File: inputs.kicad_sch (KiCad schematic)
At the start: 44 parts, among them IC3 Trig Cond Socket, U5 MPX4250, U6 SP720

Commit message: Populate Board
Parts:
- removed C15: 0.01uF, Capacitor_SMD:C_0805_2012Metric, symbol Device:C
- removed C16: 0.1uF, Capacitor_SMD:C_0805_2012Metric, symbol Device:C
- removed C29, C8: 470pf, Capacitor_SMD:C_0805_2012Metric, symbol Device:C
- removed JP4, JP5: PULL-UP, Connector_PinHeader_2.54mm:PinHeader_1x02_P2.54mm_Vertical, symbol Jumper:Jumper_2_Open
- removed R34, R55: 470R, Resistor_SMD:R_0805_2012Metric, symbol Device:R
- added C18: 0.01uF, Capacitor_SMD:C_0805_2012Metric, symbol Device:C
- added C19: 0.1uF, Capacitor_SMD:C_0805_2012Metric, symbol Device:C
- added C5, C6: 470pf, Capacitor_SMD:C_0805_2012Metric, symbol Device:C
- added JP2, JP3: PULL-UP, Connector_PinHeader_2.54mm:PinHeader_1x02_P2.54mm_Vertical, symbol Jumper:Jumper_2_Open
- JP1: renamed from JP11; footprint Jumper:SolderJumper-3_P1.3mm_Bridged12_RoundedPad1.0x1.5mm -> Jumper:SolderJumper-3_P1.3mm_Open_RoundedPad1.0x1.5mm
- renumbered C7 to C10, C5 to C11, C9 to C12, C12 to C13, C10 to C14, C13 to C15, C11 to C16, C14 to C17, C1 to C3, C2 to C4, C3 to C7, C6 to C8, C4 to C9, D20 to D2, D13 to D3, IC3 to IC1, JP2 to JP4, JP3 to JP5, R31 to R30, R29 to R31, R30 to R32, R32 to R33, R33 to R34, R38 to R35, R35 to R36, R39 to R37, R36 to R38, R40 to R39, R37 to R40
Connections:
- net ADC-Clamp-14 is gone; now on net RAW-BAT-REF: U6.15 (I14)
- net CAM-IN: now also JP3.2 (B)
- net CRANK-IN: now also JP2.1 (A)
- net GND: now also C3.2, C4.2, C18.2, C19.2, C5.2, C6.1; no longer C3.1, C4.1
- net at R41.1: now also JP2.2 (B)
- net +5VA: now reaches R42.1
- net +5VA: now also IC1.5 (Pin_5), R34.1, R36.2, R38.2, R41.2, U6.16 (V+)
- net RAW-BARO-IN: now reaches JP1.3 (B)
- net RAW-BARO-IN: now also U6.11 (I10), C6.2
- net 12V-SW renamed +12V
- net ADC-Clamp-1 renamed RAW-BAT-REF
- net RAW-BAT-REF: no longer U6.1 (I1)
- net ADC-Clamp-10 renamed RAW-FLEX-IN
- net RAW-FLEX-IN: no longer U6.11 (I10)
- net ADC-Clamp-11 renamed RAW-O2
- net RAW-O2: now also C8.1, R30.1
- net ADC-Clamp-12 renamed RAW-CAM-IN
- net RAW-CAM-IN: now also IC1.7 (Pin_7), R44.1, C19.1
- net ADC-Clamp-13 renamed RAW-CLUTCH
- net RAW-CLUTCH: now also U6.1 (I1); no longer U6.14 (I13)
- net ADC-Clamp-2 renamed RAW-COOLANT
- net RAW-COOLANT: now also C17.1, R39.1
- removed net ADC-Clamp-3: C17.1, R39.1, U6.3 (I3)
- net ADC-Clamp-4 renamed RAW-TPS
- net ADC-Clamp-5 renamed RAW-IAT
- net RAW-IAT: now also U6.14 (I13); no longer U6.5 (I5)
- removed net ADC-Clamp-6: C8.1, R30.1, U6.6 (I6)
- net ADC-Clamp-7: no longer names the net of U6.7 (I7)
- removed net ADC-Clamp-8: IC1.7 (Pin_7), R44.1, U6.9 (I8)
- net ADC-Clamp-9 renamed RAW-CRANK-IN
- net RAW-CRANK-IN: now also U6.3 (I3), C18.1; no longer U6.10 (I9)
- net CLT_Sensor renamed COOLANT-IN
- net Clutch_in renamed CLUTCH-IN
- net IAT_Sensor renamed IAT-IN
- net MAP-EXT renamed RAW-MAP-IN
- net RAW-MAP-IN: now also U6.6 (I6), C5.1
- net O2_Sensor renamed O2-IN
- net TPS_Sensor renamed TPS-IN
- removed net VDD: C3.2, C4.2, IC1.5 (Pin_5), U5.3 (VCC)
- removed net VDDA: R34.1, R36.2, R38.2, R41.2, R42.2, U6.16 (V+)
- new net: JP3.1 (A), R42.2
- new net +5V: C3.1, C4.1, U5.3 (VCC)
- new net RAW-FLEX: U6.5 (I5)
- no-connect marks 0 -> 3
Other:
- note added: "Surge Protection"
- moved on the sheet: C10, C12, C13, C14, C15, C16, C17, C3, C4, C7, C8, C9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

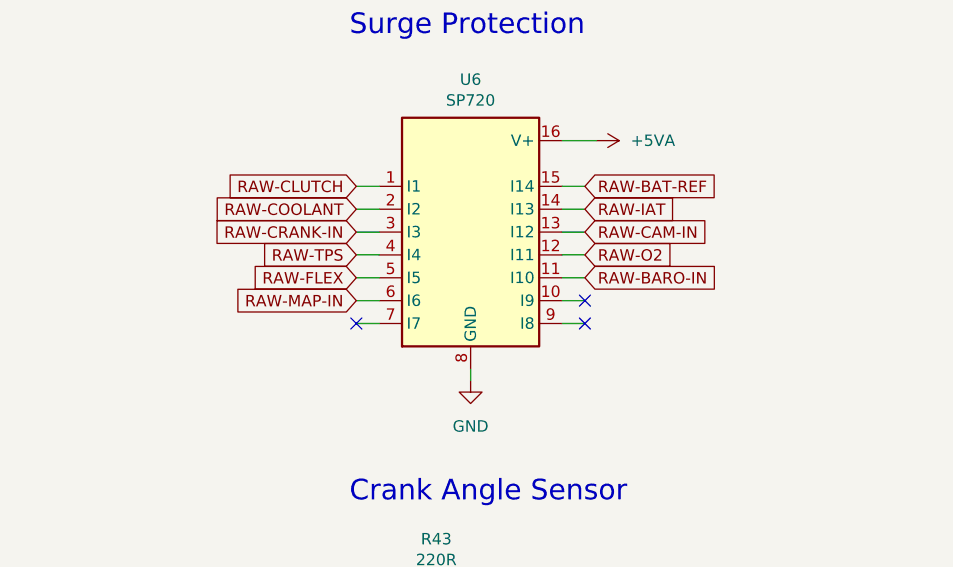
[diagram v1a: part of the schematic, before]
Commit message: Add additional IOs
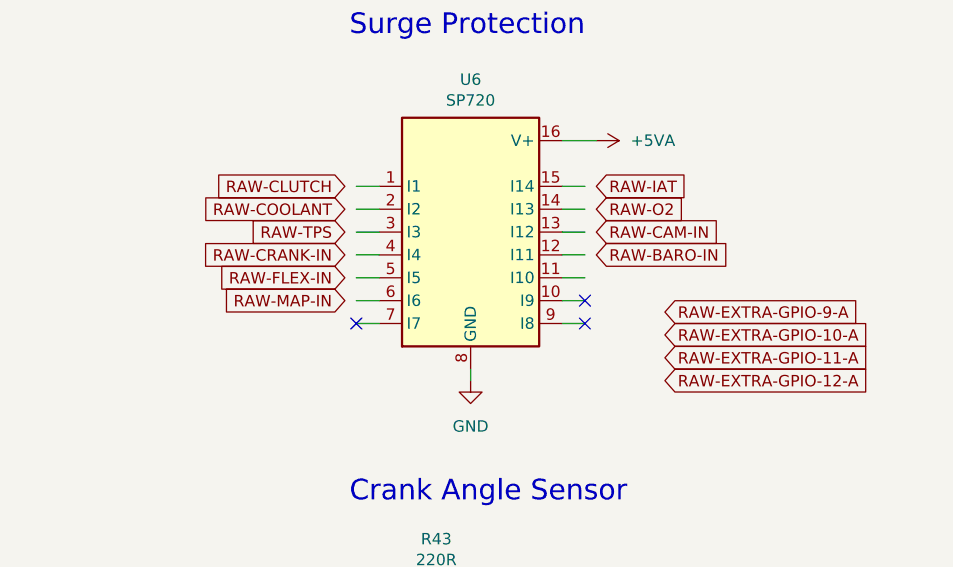
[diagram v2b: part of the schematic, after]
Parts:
- JP2, JP3: footprint Connector_PinHeader_2.54mm:PinHeader_1x02_P2.54mm_Vertical -> Jumper:SolderJumper-2_P1.3mm_Open_RoundedPad1.0x1.5mm
- JP4, JP5: footprint Connector_PinHeader_2.54mm:PinHeader_1x03_P2.54mm_Vertical -> Jumper:SolderJumper-3_P1.3mm_Open_RoundedPad1.0x1.5mm
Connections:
- net RAW-BARO-IN: no longer U6.11 (I10)
- net RAW-BAT-REF: no longer U6.15 (I14)
- net RAW-CAM-IN: no longer U6.13 (I12)
- net RAW-CLUTCH: no longer U6.1 (I1)
- net RAW-COOLANT: no longer U6.2 (I2)
- net RAW-CRANK-IN: no longer U6.3 (I3)
- net RAW-IAT: no longer U6.14 (I13)
- net RAW-MAP-IN: no longer U6.6 (I6)
- net RAW-O2: no longer U6.12 (I11)
- net RAW-TPS: no longer U6.4 (I4)
- net RAW-FLEX: no longer names the net of U6.5 (I5)
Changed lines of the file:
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@@
 		)
 	)
-	(global_label "RAW-CRANK-IN"
+	(global_label "RAW-BARO-IN"
 		(shape input)
-		(at 215.9 48.26 180)
+		(at 242.57 50.8 0)
 		(effects
 			(font
 				(size 1.27 1.27)
 			)
-			(justify right)
+			(justify left)
 		)
 		(property "Intersheetrefs" "${INTERSHEET_REFS}"
-			(at 215.9 48.26 0)
+			(at 242.57 50.8 0)
 			(effects
 				(font
@@
 		)
 	)
-	(global_label "RAW-CLUTCH"
+	(global_label "RAW-BAT-REF"
 		(shape input)
-		(at 215.9 43.18 180)
+		(at 72.39 128.27 0)
 		(effects
 			(font
 				(size 1.27 1.27)
 			)
-			(justify right)
+			(justify left)
 		)
 		(property "Intersheetrefs" "${INTERSHEET_REFS}"
-			(at 215.9 43.18 0)
+			(at 72.39 128.27 0)
 			(effects
 				(font
@@
 		)
 	)
-	(global_label "RAW-MAP-IN"
+	(global_label "RAW-COOLANT"
 		(shape input)
-		(at 215.9 55.88 180)
+		(at 214.63 45.72 180)
 		(effects
 			(font
@@
 		)
 		(property "Intersheetrefs" "${INTERSHEET_REFS}"
-			(at 215.9 55.88 0)
+			(at 214.63 45.72 0)
 			(effects
 				(font
 					(size 1.27 1.27)
 				)
-				(justify left)
 				(hide yes)
 			)
 		)
 	)
-	(global_label "RAW-IAT"
+	(global_label "RAW-COOLANT"
 		(shape input)
-		(at 241.3 45.72 0)
+		(at 144.78 125.73 0)
 		(effects
 			(font
@@
 		)
 		(property "Intersheetrefs" "${INTERSHEET_REFS}"
-			(at 241.3 45.72 0)
+			(at 144.78 125.73 0)
 			(effects
 				(font
 					(size 1.27 1.27)
 				)
-				(justify right)
 				(hide yes)
 			)
 		)
 	)
-	(global_label "RAW-COOLANT"
+	(global_label "VR1-"
 		(shape input)
-		(at 144.78 125.73 0)
+		(at 229.87 102.87 180)
 		(effects
 			(font
 				(size 1.27 1.27)
 			)
-			(justify left)
+			(justify right)
 		)
 		(property "Intersheetrefs" "${INTERSHEET_REFS}"
-			(at 144.78 125.73 0)
+			(at 229.87 102.87 0)
 			(effects
 				(font
@@
 		)
 	)
-	(global_label "RAW-CAM-IN"
+	(global_label "RAW-CRANK-IN"
 		(shape input)
-		(at 241.3 48.26 0)
+		(at 214.63 50.8 180)
 		(effects
 			(font
 				(size 1.27 1.27)
 			)
-			(justify left)
+			(justify right)
 		)
 		(property "Intersheetrefs" "${INTERSHEET_REFS}"
-			(at 241.3 48.26 0)
+			(at 214.63 50.8 0)
 			(effects
 				(font
 					(size 1.27 1.27)
 				)
-				(justify left)
+				(justify right)
 				(hide yes)
 			)
 		)
 	)
-	(global_label "VR1-"
+	(global_label "RAW-CLUTCH"
 		(shape input)
-		(at 229.87 102.87 180)
+		(at 140.97 165.1 0)
 		(effects
 			(font
 				(size 1.27 1.27)
 			)
-			(justify right)
+			(justify left)
 		)
 		(property "Intersheetrefs" "${INTERSHEET_REFS}"
-			(at 229.87 102.87 0)
+			(at 140.97 165.1 0)
 			(effects
 				(font
@@
 		)
 	)
-	(global_label "RAW-O2"
+	(global_label "RAW-EXTRA-GPIO-10-A"
 		(shape input)
-		(at 241.3 50.8 0)
+		(at 250.19 59.69 0)
 		(effects
 			(font
@@
 		)
 		(property "Intersheetrefs" "${INTERSHEET_REFS}"
-			(at 241.3 50.8 0)
+			(at 250.19 59.69 0)
 			(effects
 				(font
 					(size 1.27 1.27)
 				)
-				(justify right)
 				(hide yes)
 			)
@@
 	(global_label "RAW-CLUTCH"
 		(shape input)
-		(at 140.97 165.1 0)
+		(at 214.63 43.18 180)
 		(effects
 			(font
 				(size 1.27 1.27)
 			)
-			(justify left)
+			(justify right)
 		)
 		(property "Intersheetrefs" "${INTERSHEET_REFS}"
-			(at 140.97 165.1 0)
+			(at 214.63 43.18 0)
 			(effects
 				(font
@@
 		)
 	)
-	(global_label "RAW-BARO-IN"
+	(global_label "IAT-IN"
 		(shape input)
-		(at 241.3 53.34 0)
+		(at 116.84 78.74 180)
 		(effects
 			(font
 				(size 1.27 1.27)
 			)
-			(justify left)
+			(justify right)
 		)
 		(property "Intersheetrefs" "${INTERSHEET_REFS}"
-			(at 241.3 53.34 0)
+			(at 116.84 78.74 0)
 			(effects
 				(font
 					(size 1.27 1.27)
 				)
-				(justify right)
 				(hide yes)
 			)
 		)
 	)
-	(global_label "IAT-IN"
+	(global_label "RAW-EXTRA-GPIO-12-A"
 		(shape input)
-		(at 116.84 78.74 180)
+		(at 250.19 64.77 0)
 		(effects
 			(font
 				(size 1.27 1.27)
 			)
-			(justify right)
+			(justify left)
 		)
 		(property "Intersheetrefs" "${INTERSHEET_REFS}"
-			(at 116.84 78.74 0)
+			(at 250.19 64.77 0)
 			(effects
 				(font
@@
 		)
 	)
-	(global_label "RAW-BAT-REF"
+	(global_label "RAW-EXTRA-GPIO-11-A"
 		(shape input)
-		(at 72.39 128.27 0)
+		(at 250.19 62.23 0)
 		(effects
 			(font
@@
 		)
 		(property "Intersheetrefs" "${INTERSHEET_REFS}"
-			(at 72.39 128.27 0)
+			(at 250.19 62.23 0)
 			(effects
 				(font
@@
 		)
 	)
-	(global_label "RAW-BAT-REF"
+	(global_label "RAW-CAM-IN"
 		(shape input)
-		(at 241.3 43.18 0)
+		(at 242.57 48.26 0)
 		(effects
 			(font
@@
 		)
 		(property "Intersheetrefs" "${INTERSHEET_REFS}"
-			(at 241.3 43.18 0)
+			(at 242.57 48.26 0)
+			(effects
+				(font
+					(size 1.27 1.27)
+				)
+				(justify left)
+				(hide yes)
+			)
+		)
+	)
+	(global_label "RAW-FLEX-IN"
+		(shape input)
+		(at 214.63 53.34 180)
+		(effects
+			(font
+				(size 1.27 1.27)
+			)
+			(justify right)
+		)
+		(property "Intersheetrefs" "${INTERSHEET_REFS}"
+			(at 214.63 53.34 0)
 			(effects
 				(font
 					(size 1.27 1.27)
 				)
-				(justify right)
 				(hide yes)
 			)
@@
 		)
 	)
-	(global_label "RAW-FLEX"
+	(global_label "RAW-TPS"
 		(shape input)
-		(at 215.9 53.34 180)
+		(at 214.63 48.26 180)
 		(effects
 			(font
@@
 		)
 		(property "Intersheetrefs" "${INTERSHEET_REFS}"
-			(at 215.9 53.34 0)
+			(at 214.63 48.26 0)
 			(effects
 				(font
 					(size 1.27 1.27)
 				)
+				(justify left)
 				(hide yes)
 			)
@@
 		)
 	)
-	(global_label "RAW-TPS"
+	(global_label "RAW-O2"
 		(shape input)
-		(at 215.9 50.8 180)
+		(at 242.57 45.72 0)
 		(effects
 			(font
 				(size 1.27 1.27)
 			)
-			(justify right)
+			(justify left)
 		)
 		(property "Intersheetrefs" "${INTERSHEET_REFS}"
-			(at 215.9 50.8 0)
+			(at 242.57 45.72 0)
 			(effects
 				(font
 					(size 1.27 1.27)
 				)
-				(justify left)
+				(justify right)
 				(hide yes)
 			)
@@
 		)
 	)
+	(global_label "RAW-EXTRA-GPIO-9-A"
+		(shape input)
+		(at 250.19 57.15 0)
+		(effects
+			(font
+				(size 1.27 1.27)
+			)
+			(justify left)
+		)
+		(property "Intersheetrefs" "${INTERSHEET_REFS}"
+			(at 250.19 57.15 0)
+			(effects
+				(font
+					(size 1.27 1.27)
+				)
+				(hide yes)
+			)
+		)
+	)
 	(global_label "COOLANT-IN"
 		(shape input)
@@
 		)
 	)
+	(global_label "RAW-MAP-IN"
+		(shape input)
+		(at 214.63 55.88 180)
+		(effects
+			(font
+				(size 1.27 1.27)
+			)
+			(justify right)
+		)
+		(property "Intersheetrefs" "${INTERSHEET_REFS}"
+			(at 214.63 55.88 0)
+			(effects
+				(font
+					(size 1.27 1.27)
+				)
+				(justify left)
+				(hide yes)
+			)
+		)
+	)
 	(global_label "RAW-IAT"
 		(shape input)
@@
 		)
 	)
-	(global_label "RAW-COOLANT"
+	(global_label "RAW-IAT"
 		(shape input)
-		(at 215.9 45.72 180)
+		(at 242.57 43.18 0)
 		(effects
 			(font
 				(size 1.27 1.27)
 			)
-			(justify right)
+			(justify left)
 		)
 		(property "Intersheetrefs" "${INTERSHEET_REFS}"
-			(at 215.9 45.72 0)
+			(at 242.57 43.18 0)
 			(effects
 				(font
 					(size 1.27 1.27)
 				)
+				(justify right)
 				(hide yes)
 			)
@@
 			)
 		)
-		(property "Footprint" "Connector_PinHeader_2.54mm:PinHeader_1x03_P2.54mm_Vertical"
+		(property "Footprint" "Jumper:SolderJumper-3_P1.3mm_Open_RoundedPad1.0x1.5mm"
 			(at 218.44 96.52 0)
 			(effects
@@
 			)
 		)
-		(property "Footprint" "Connector_PinHeader_2.54mm:PinHeader_1x03_P2.54mm_Vertical"
+		(property "Footprint" "Jumper:SolderJumper-3_P1.3mm_Open_RoundedPad1.0x1.5mm"
 			(at 218.44 116.84 0)
 			(effects
@@
 			)
 		)
-		(property "Footprint" "Connector_PinHeader_2.54mm:PinHeader_1x02_P2.54mm_Vertical"
+		(property "Footprint" "Jumper:SolderJumper-2_P1.3mm_Open_RoundedPad1.0x1.5mm"
 			(at 204.47 116.84 0)
 			(effects
@@
 			)
 		)
-		(property "Footprint" "Connector_PinHeader_2.54mm:PinHeader_1x02_P2.54mm_Vertical"
+		(property "Footprint" "Jumper:SolderJumper-2_P1.3mm_Open_RoundedPad1.0x1.5mm"
 			(at 204.47 96.52 0)
 			(effects

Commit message: Pre MCU switch
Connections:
- net RAW-BARO-IN: now also U6.7 (I7)
- net RAW-CAM-IN: now also U6.5 (I5)
- net RAW-CLUTCH: now also U6.10 (I9)
- net RAW-COOLANT: now also U6.3 (I3)
- net RAW-CRANK-IN: now also U6.4 (I4)
- net RAW-EXTRA-GPIO-10-A: now also U6.13 (I12)
- net RAW-EXTRA-GPIO-11-A: now also U6.14 (I13)
- net RAW-EXTRA-GPIO-12-A: now also U6.15 (I14)
- net RAW-EXTRA-GPIO-9-A: now also U6.12 (I11)
- net RAW-FLEX-IN: now also U6.2 (I2)
- net RAW-IAT: now also U6.11 (I10)
- net RAW-MAP-IN: now also U6.6 (I6)
- net RAW-O2: now also U6.1 (I1)
- net RAW-TPS: now also U6.9 (I8)
- no-connect marks 3 -> 0

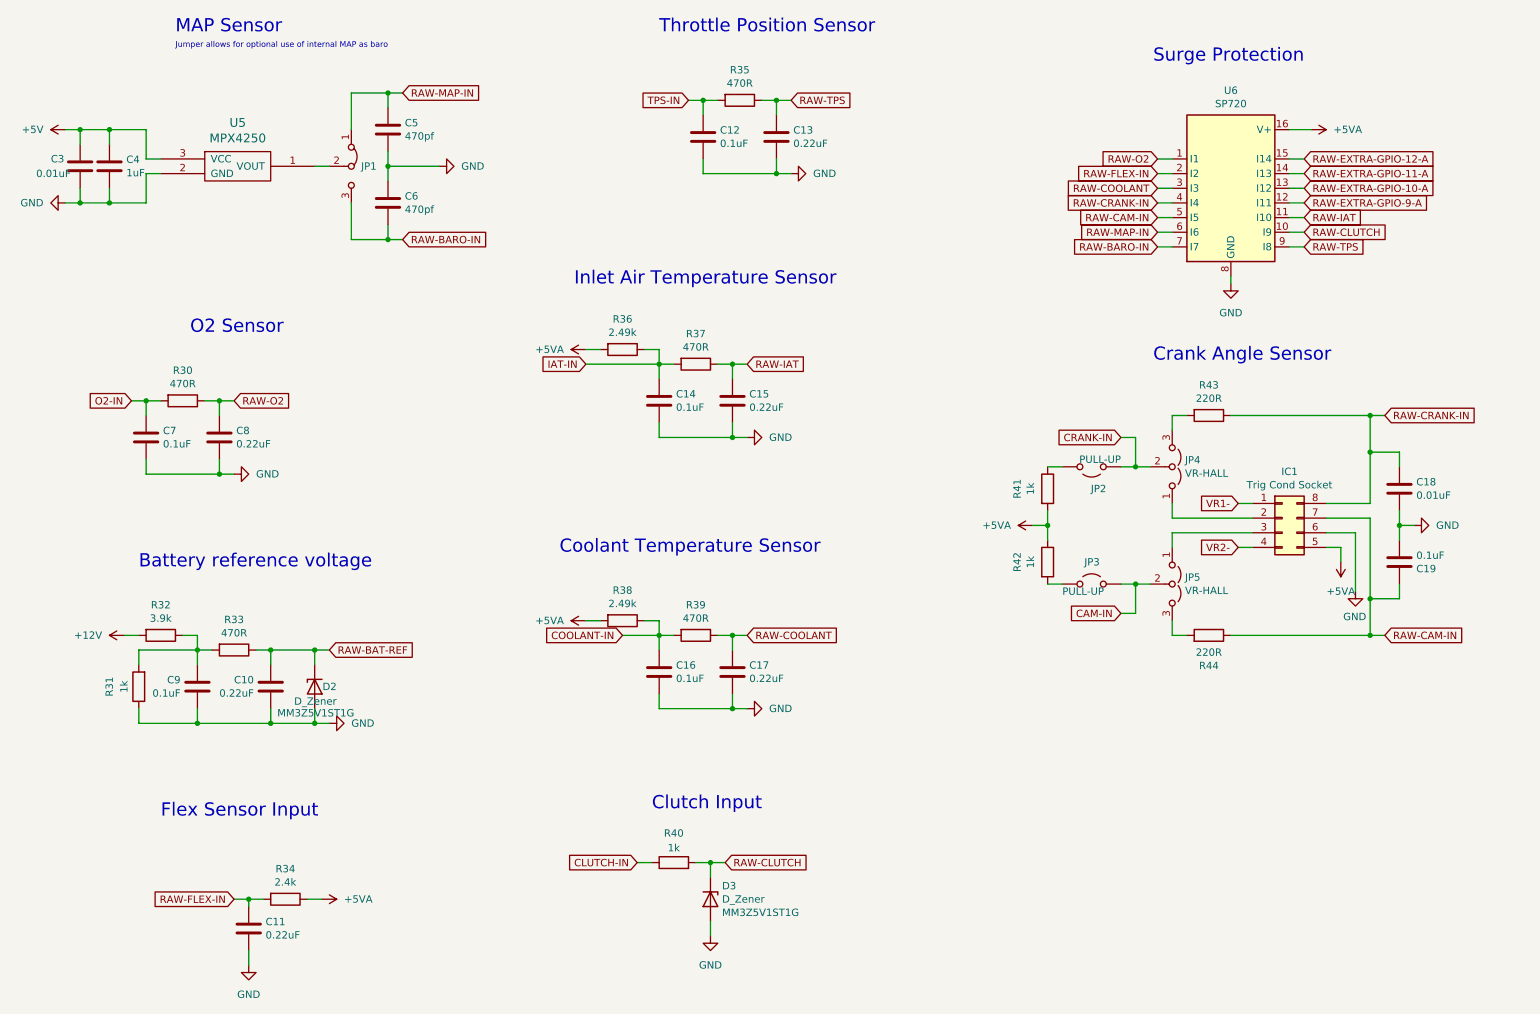
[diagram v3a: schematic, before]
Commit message: Update from Speeduino Discord suggestions (thanks to Detonator)
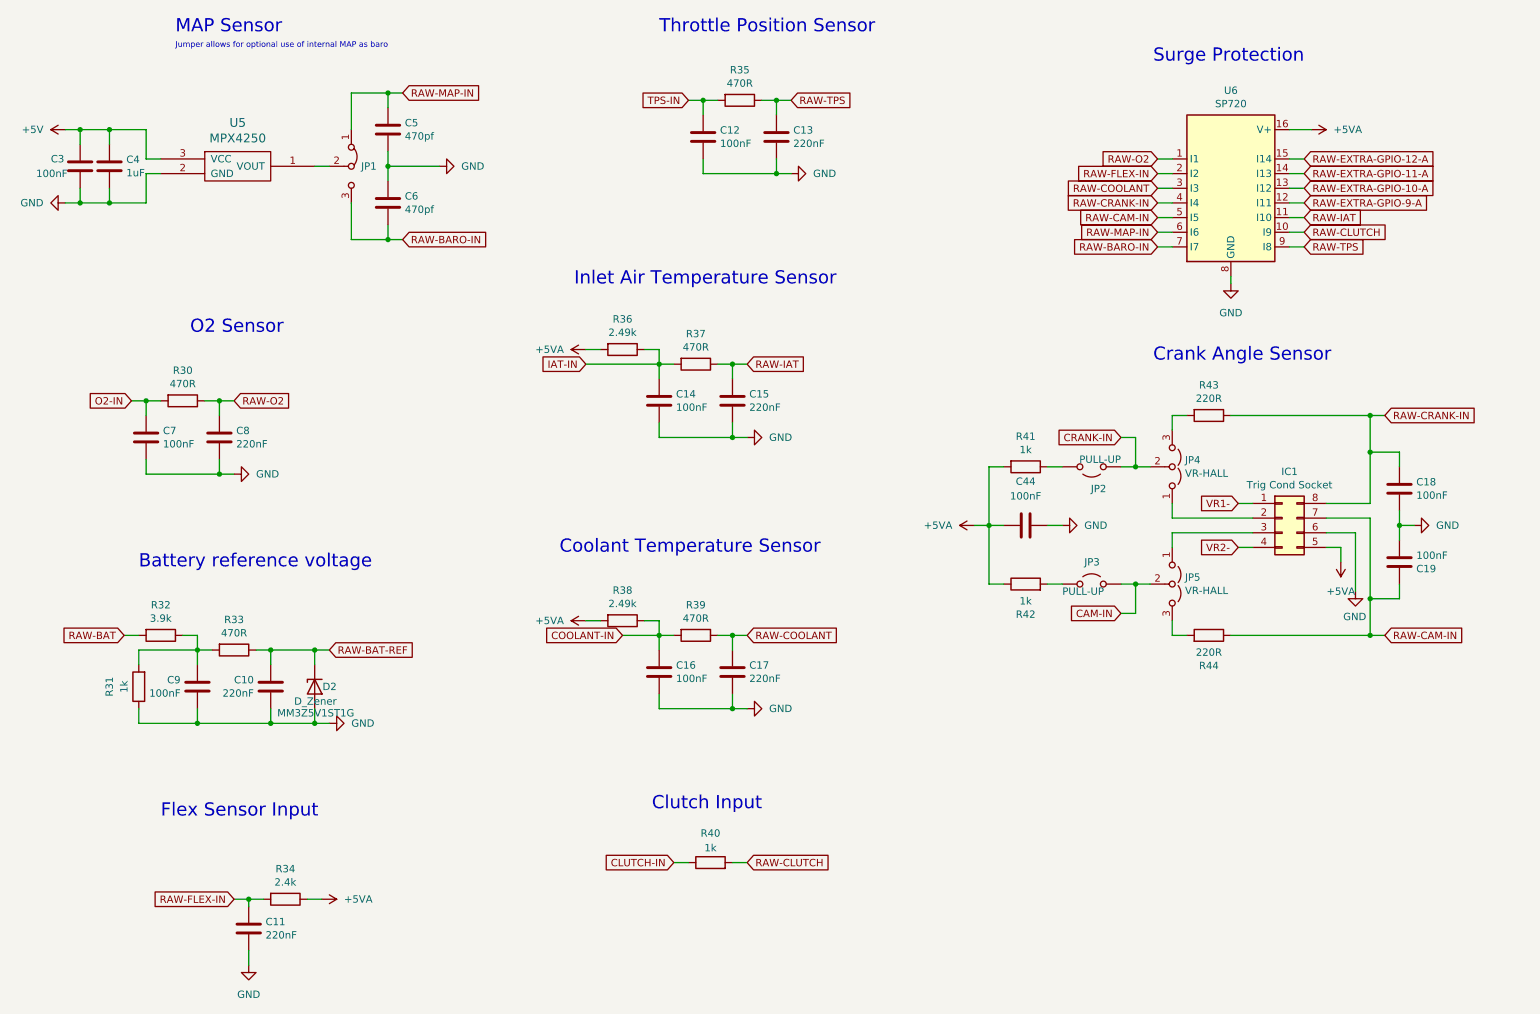
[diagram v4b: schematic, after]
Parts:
- removed D3: D_Zener, Diode_SMD:D_SOD-323, symbol Device:D_Zener
- added C44: 100nF, Capacitor_SMD:C_0805_2012Metric, symbol Device:C
- C10, C11, C13, C15, C17, C8: value 0.22uF -> 220nF
- C12, C14, C16, C19, C7, C9: value 0.1uF -> 100nF
- C18, C3: value 0.01uF -> 100nF
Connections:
- net +5VA: now also C44.1
- net GND: now also C44.2
- net +12V renamed RAW-BAT
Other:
- moved on the sheet: R40, R41, R42

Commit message: Fully connect all components
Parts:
- removed C10, C11, C13, C15, C17, C8: 220nF, Capacitor_SMD:C_0805_2012Metric, symbol Device:C
- R34: value 2.4k -> 2.49k
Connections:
- net +5VA: now also R34.2; no longer R34.1
- net CLUTCH-IN renamed CLUTCH-HZ-IN
- net RAW-BARO-IN renamed BARO-HZ-IN
- net BARO-HZ-IN: now also U6.2 (I2); no longer U6.7 (I7)
- net RAW-BAT renamed VBAT
- net RAW-BAT-REF renamed BAT-REF-HZ
- net RAW-CAM-IN renamed CAM-HZ-IN
- net CAM-HZ-IN: now also U6.3 (I3); no longer U6.5 (I5)
- net RAW-CLUTCH renamed CLUTCH-HZ
- net RAW-COOLANT renamed COOLANT-HZ
- net COOLANT-HZ: now also U6.6 (I6); no longer U6.3 (I3)
- net RAW-CRANK-IN renamed CRANK-HZ-IN
- net RAW-EXTRA-GPIO-10-A renamed EXTRA-GPIO-10-HZ-A
- net RAW-EXTRA-GPIO-11-A renamed EXTRA-GPIO-11-HZ-A
- net RAW-EXTRA-GPIO-12-A renamed EXTRA-GPIO-12-HZ-A
- net RAW-EXTRA-GPIO-9-A renamed EXTRA-GPIO-9-HZ-A
- removed net RAW-FLEX-IN: R34.2, U6.2 (I2)
- net RAW-IAT renamed FLEX-HZ-IN
- net FLEX-HZ-IN: now also R34.1; no longer R37.1
- net RAW-MAP-IN renamed MAP-HZ-IN
- net MAP-HZ-IN: now also U6.1 (I1); no longer U6.6 (I6)
- net RAW-O2 renamed O2-HZ
- net O2-HZ: now also U6.7 (I7); no longer U6.1 (I1)
- net RAW-TPS renamed TPS-HZ
- new net IAT-HZ: R37.1, U6.5 (I5)
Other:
- moved on the sheet: D2, R34
